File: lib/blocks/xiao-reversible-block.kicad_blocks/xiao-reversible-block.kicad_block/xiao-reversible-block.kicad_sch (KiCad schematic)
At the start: 34 parts, among them J1 Conn_01x02, U1 XIAO-nRF52840-DIP

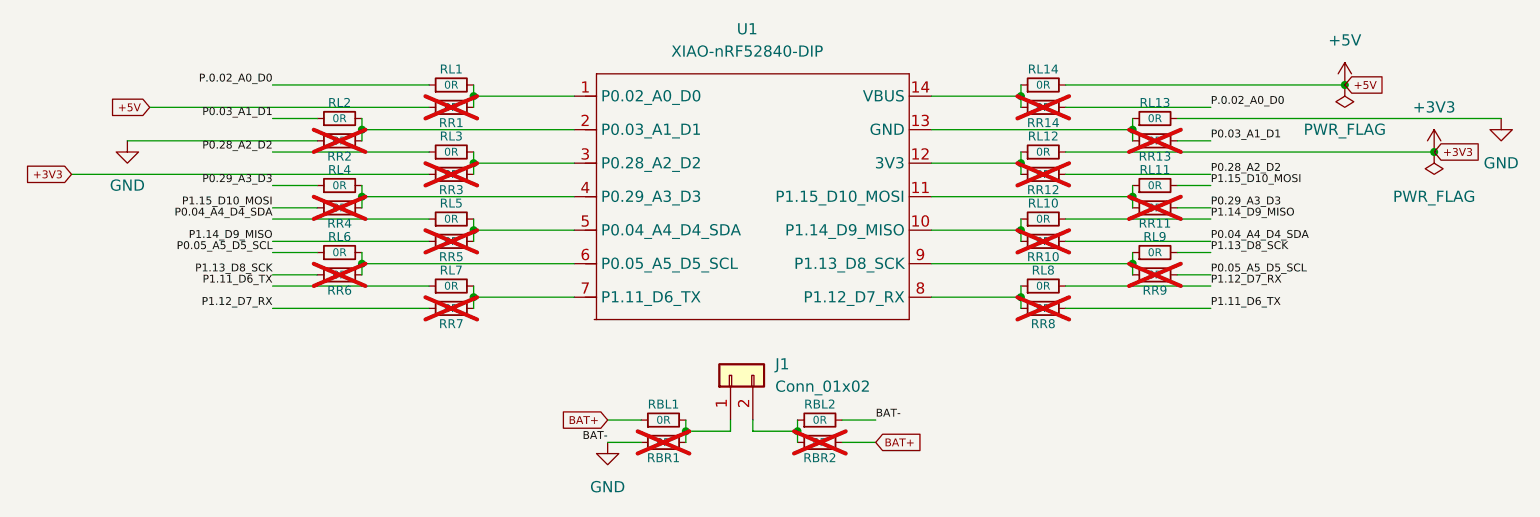
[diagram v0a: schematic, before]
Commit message: fix: decrease header spacing, remove JST battery connector
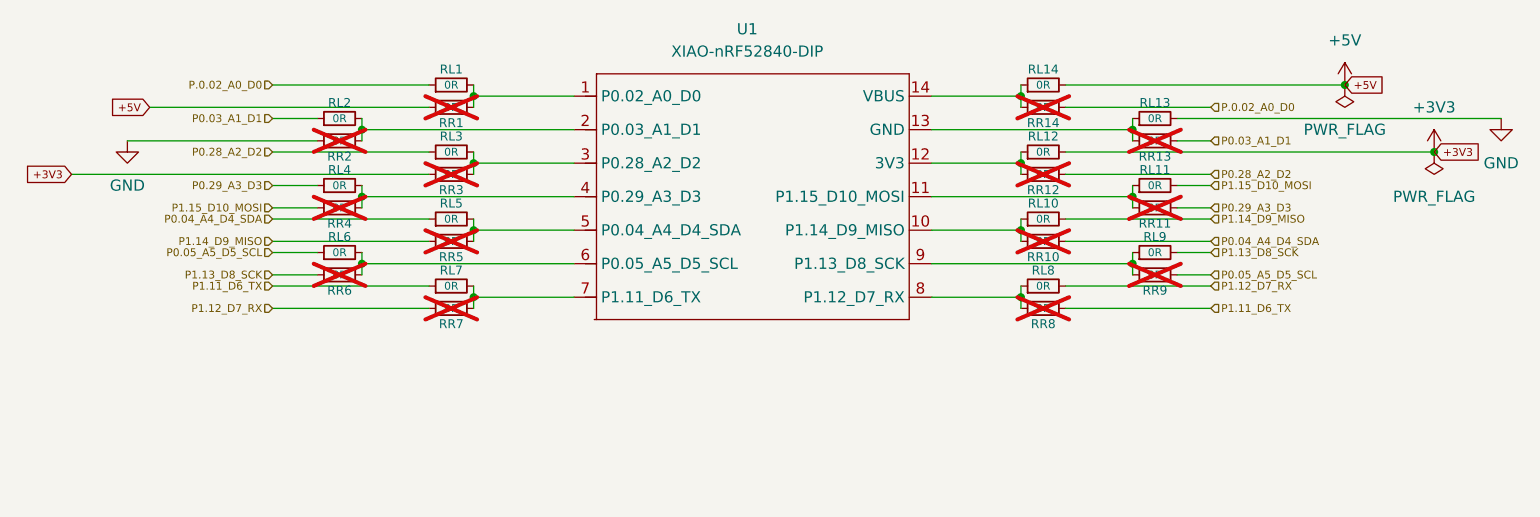
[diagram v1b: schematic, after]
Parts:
- removed J1: Conn_01x02, Connector_JST:JST_PH_S2B-PH-K_1x02_P2.00mm_Horizontal, symbol Connector_Generic:Conn_01x02
- removed RBL1, RBL2, RBR1, RBR2: 0R, symbol Device:R_Small
- RL1, RL10, RL11, RL12, RL13, RL14, RL2, RL3, RL4, RL5, RL6, RL7, RL8, RL9, RR1, RR10, RR11, RR12, RR13, RR14, RR2, RR3, RR4, RR5, RR6, RR7, RR8, RR9: footprint (none) -> xiao-reversible-block:R_0603_1608Metric_Pad0.98x0.95mm_HandSolder_0R
